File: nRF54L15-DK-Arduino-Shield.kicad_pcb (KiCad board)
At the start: 2 copper layers, 62 x 55.4 mm, 15 parts

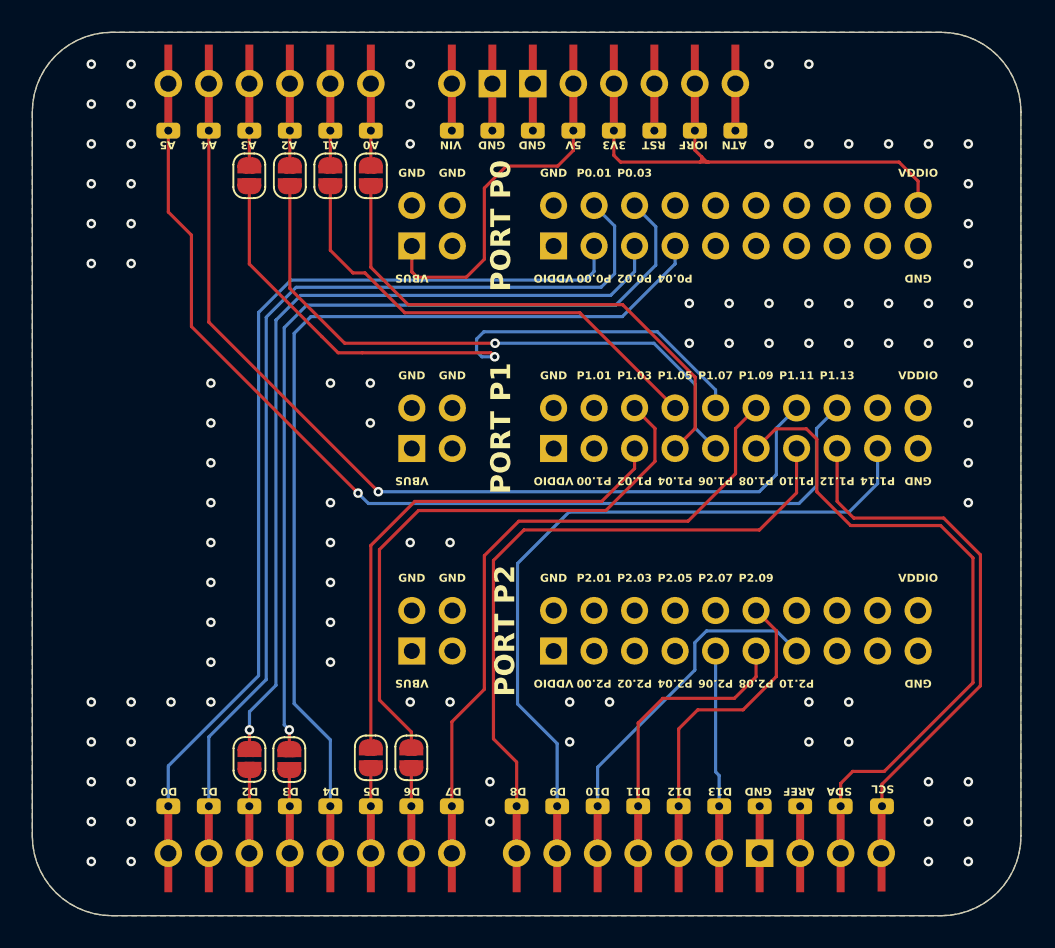
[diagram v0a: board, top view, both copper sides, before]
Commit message: Updates for LR1110 Arduino shield
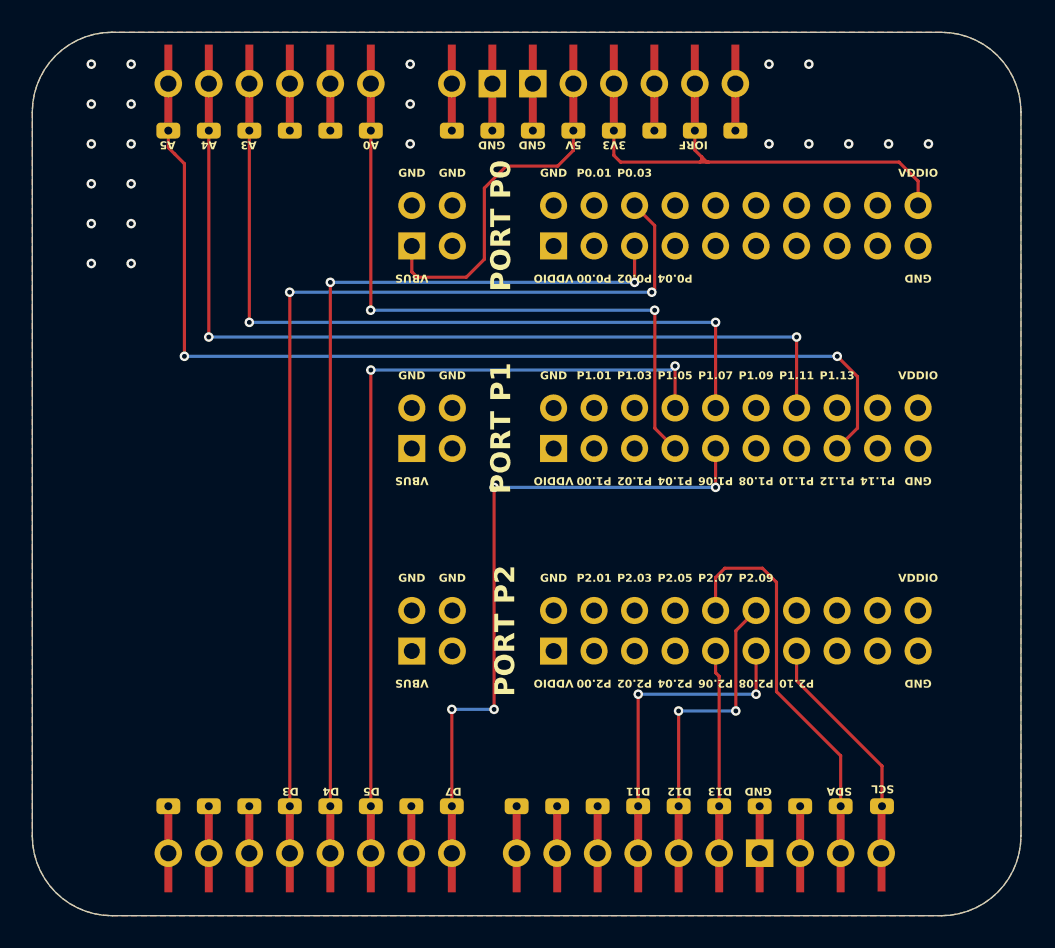
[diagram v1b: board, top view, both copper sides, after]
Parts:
- removed JP1, JP2, JP3, JP4, JP5, JP6, JP7, JP8: SolderJumper_2_Open, Jumper:SolderJumper-2_P1.3mm_Open_RoundedPad1.0x1.5mm
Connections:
- A1 pad A0: Net-(JP5-A) -> /P1.04
- A1 pad A1: Net-(JP6-A) -> unconnected-(A1-PadA1)_2
- A1 pad A2: Net-(JP7-A) -> unconnected-(A1-PadA2)_3
- A1 pad A3: Net-(JP8-A) -> /P1.07
- A1 pad A5: /P1.13 -> /P1.12
- A1 pad D0: /P0.00 -> unconnected-(A1-D0/RX-PadD0)
- A1 pad D1: /P0.01 -> unconnected-(A1-D1/TX-PadD1)_2
- A1 pad D10: /P2.10 -> unconnected-(A1-D10_CS-PadD10)_1
- A1 pad D2: Net-(JP3-A) -> unconnected-(A1-PadD2)
- A1 pad D3: Net-(JP4-A) -> /P0.03
- A1 pad D4: /P0.04 -> /P0.02
- A1 pad D5: Net-(JP1-A) -> /P1.05
- A1 pad D6: Net-(JP2-A) -> unconnected-(A1-PadD6)_2
- A1 pad D7: /P1.09 -> /P1.06
- A1 pad D8: /P1.10 -> unconnected-(A1-PadD8)_1
- A1 pad D9: /P1.14 -> unconnected-(A1-PadD9)_1
- A1 pad SCL: /P1.12 -> /P2.10
- A1 pad SDA: /P1.08 -> /P2.07
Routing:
- net /P1.13: track 62.6 -> 0.00 mm, vias 1 -> 0
- net /P0.01: track 59.9 -> 0.00 mm
- net /P0.04: track 57.4 -> 0.00 mm
- net /P0.00: track 57.0 -> 0.00 mm
- net /P1.14: track 43.1 -> 0.00 mm
- net /P1.10: track 39.6 -> 0.00 mm
- net /P1.08: track 39.6 -> 0.00 mm
- net /P1.09: track 39.1 -> 0.00 mm
- net /P1.03: track 36.7 -> 0.00 mm
- net /P1.02: track 32.5 -> 0.00 mm
- net /P1.12: track 32.0 -> 62.3 mm, vias 0 -> 2
- net /P2.07: track 0.00 -> 22.2 mm
- net /P1.05: track 29.7 -> 49.2 mm, vias 0 -> 2
- net /P2.10: track 20.0 -> 12.0 mm
- net /P0.03: track 55.8 -> 61.0 mm, vias 1 -> 2
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
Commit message: Added VDD jumper
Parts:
- added J1: Conn_01x02, Connector_PinHeader_2.54mm:PinHeader_1x02_P2.54mm_Vertical, F.Cu at (200.7, 88.9)
- added JP1: SolderJumper_2_Open, Jumper:SolderJumper-2_P1.3mm_Open_RoundedPad1.0x1.5mm, F.Cu at (200.7, 92.0)
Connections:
- GPIO0 pad 20: +3.3V -> Net-(GPIO0-Pin_20)
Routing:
- net +3.3V: track 25.6 -> 40.7 mm, vias 0 -> 1
- net Net-(GPIO0-Pin_20): track 0.00 -> 8.99 mm
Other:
- board text added: "VDD Jumper"
